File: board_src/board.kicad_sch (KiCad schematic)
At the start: 42 parts, among them J1 Conn_01x05, J16 Conn_01x05, J17 Conn_01x05, J18 Conn_02x20_Counter_Clockwise, J2 Conn_01x05, J20 Conn_02x20_Counter_Clockwise, J21 Conn_02x20_Counter_Clockwise, J22 Conn_02x20_Counter_Clockwise, J26 Conn_01x20_Socket, J27 Conn_01x20_Socket, J30 Conn_01x05, J31 Conn_01x05, J36 Conn_01x20_Socket, J37 Conn_01x20_Socket, J40 Conn_01x01_Pin, J41 Conn_01x01_Pin, J42 Conn_01x01_Pin, J43 Conn_01x01_Pin, J44 Conn_01x01_Pin, J46 Conn_01x01_Pin, U1 Pico, U4 Pico

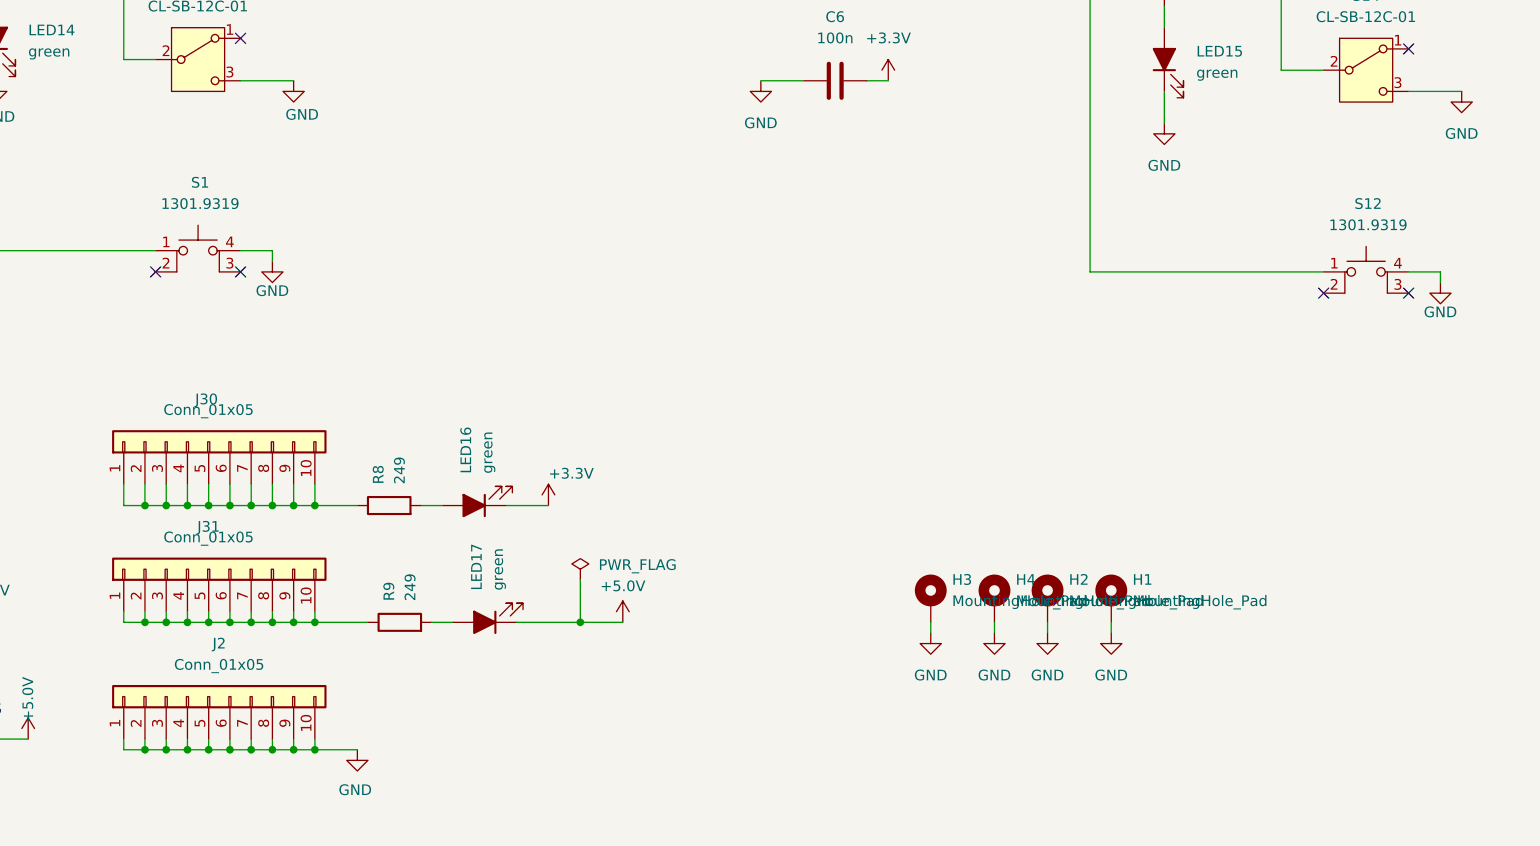
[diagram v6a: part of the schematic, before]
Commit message: poprawione polaczenia diod i wartosci opornikow, aktualizacja niektorych elementow ze wzgledu na braki w magazynie
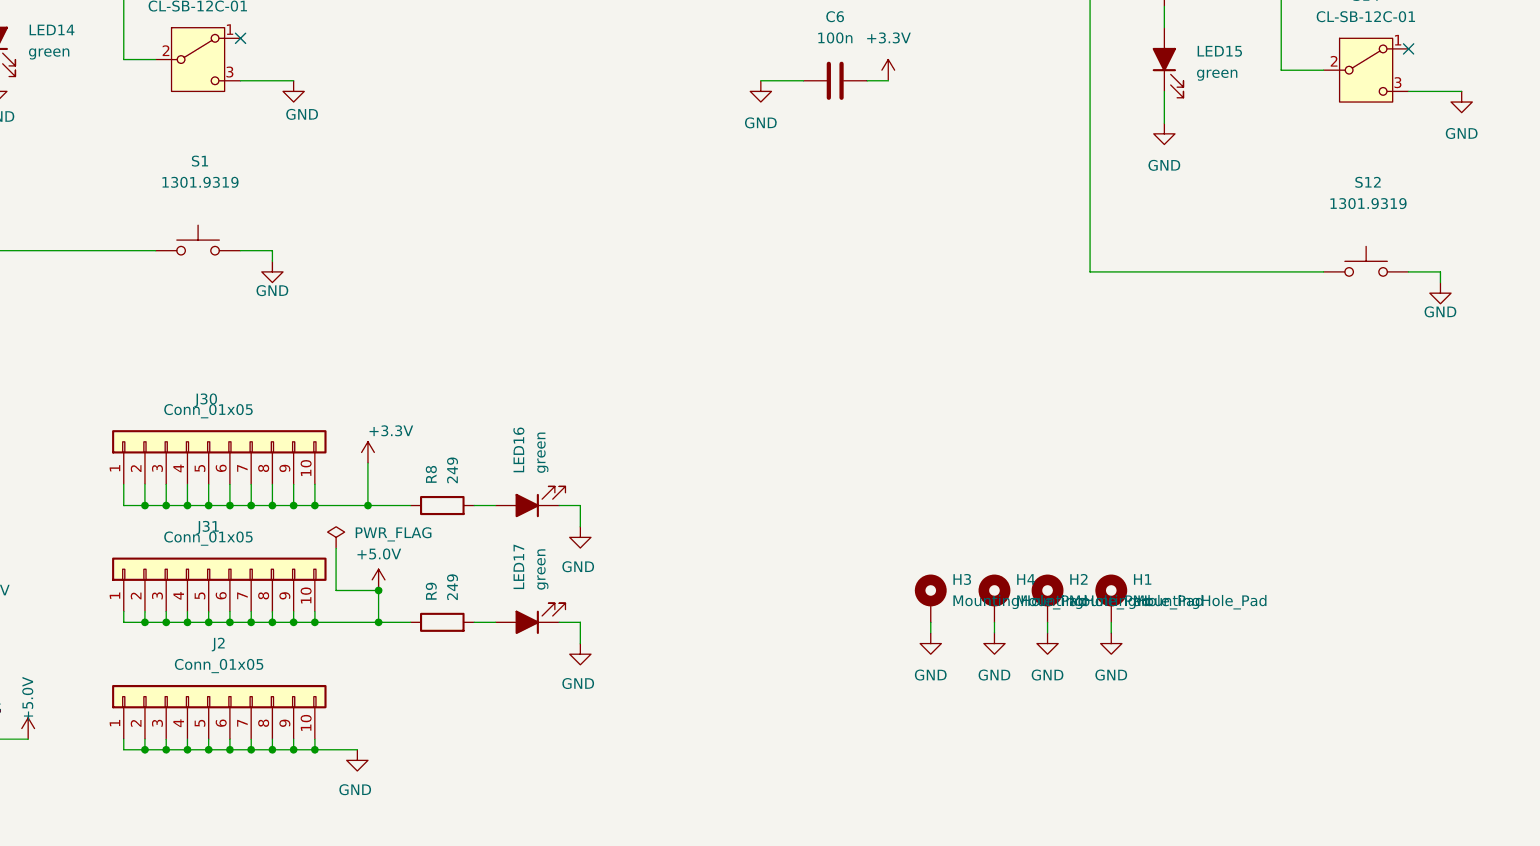
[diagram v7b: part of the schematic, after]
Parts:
- S1, S12: symbol Switch:SW_MEC_5E -> Switch:SW_Push
- S11, S14: footprint footprints:CLSB12C01 -> footprints:JS102011CQN
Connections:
- net +3.3V: now also J30.1 (Pin_1), J30.10 (Pin_10), J30.2 (Pin_2), J30.3 (Pin_3), J30.4 (Pin_4), J30.5 (Pin_5), J30.6 (Pin_6), J30.7 (Pin_7), J30.8 (Pin_8), J30.9 (Pin_9), R8.1; no longer LED16.1 (K)
- net +5.0V: now also J31.1 (Pin_1), J31.10 (Pin_10), J31.2 (Pin_2), J31.3 (Pin_3), J31.4 (Pin_4), J31.5 (Pin_5), J31.6 (Pin_6), J31.7 (Pin_7), J31.8 (Pin_8), J31.9 (Pin_9), R9.1; no longer LED17.1 (K)
- net GND: now also LED16.1 (K), LED17.1 (K), S1.2, S12.2; no longer S1.4 (A), S12.4 (A)
- no-connect marks 92 -> 88
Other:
- moved on the sheet: LED16, LED17, R8, R9

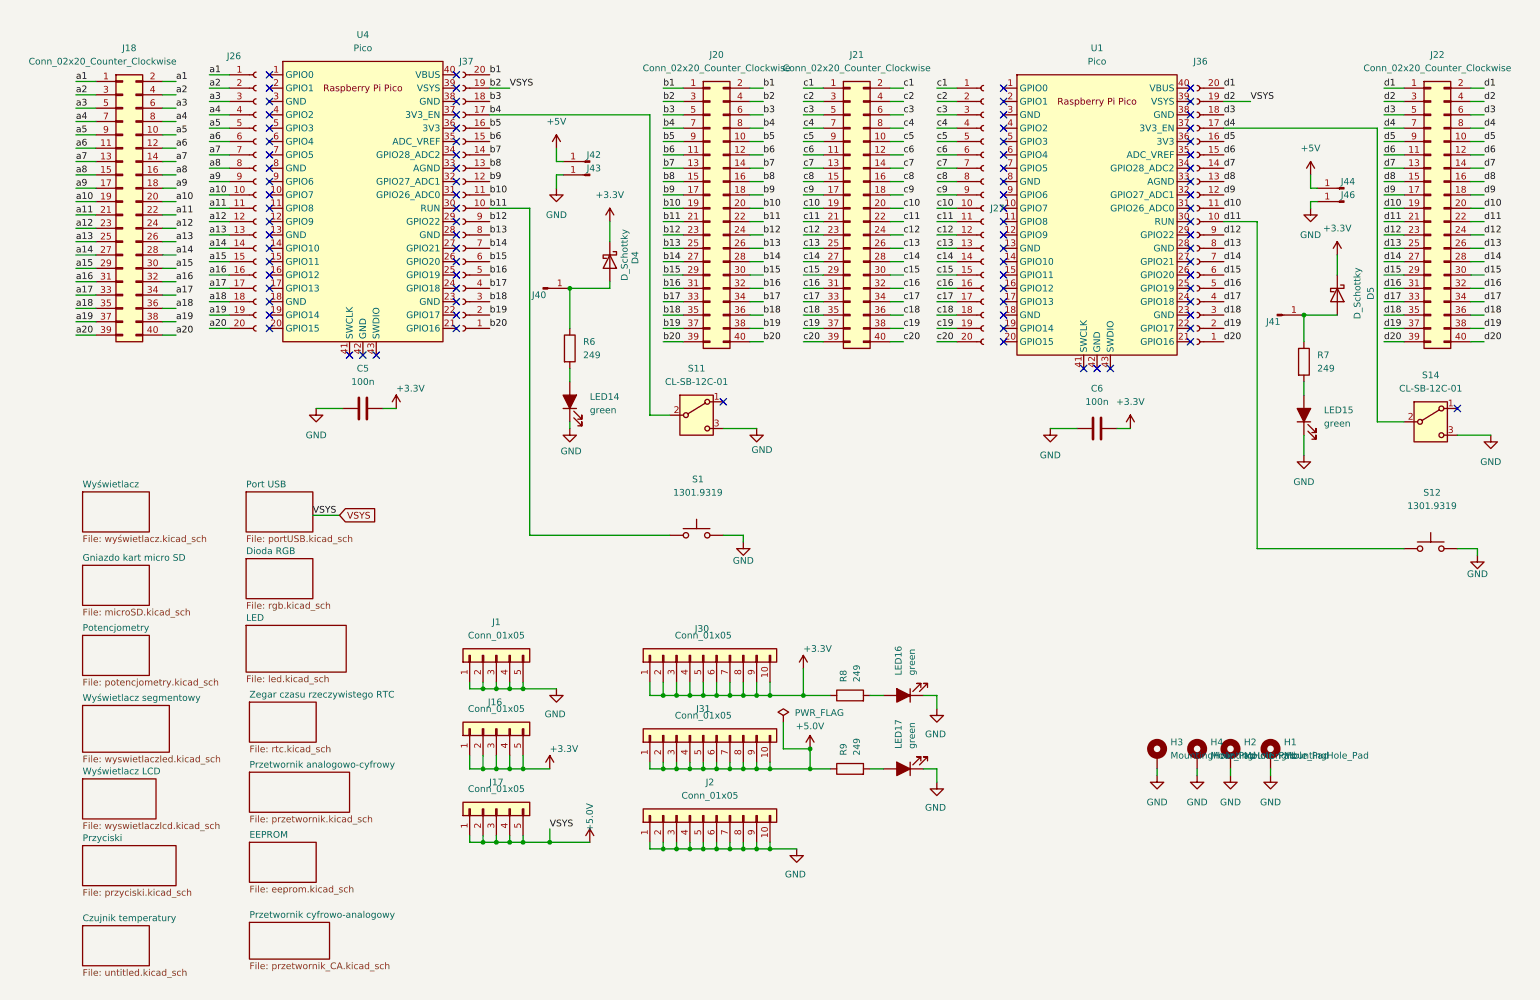
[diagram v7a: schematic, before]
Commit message: dodany tranzystor BS123
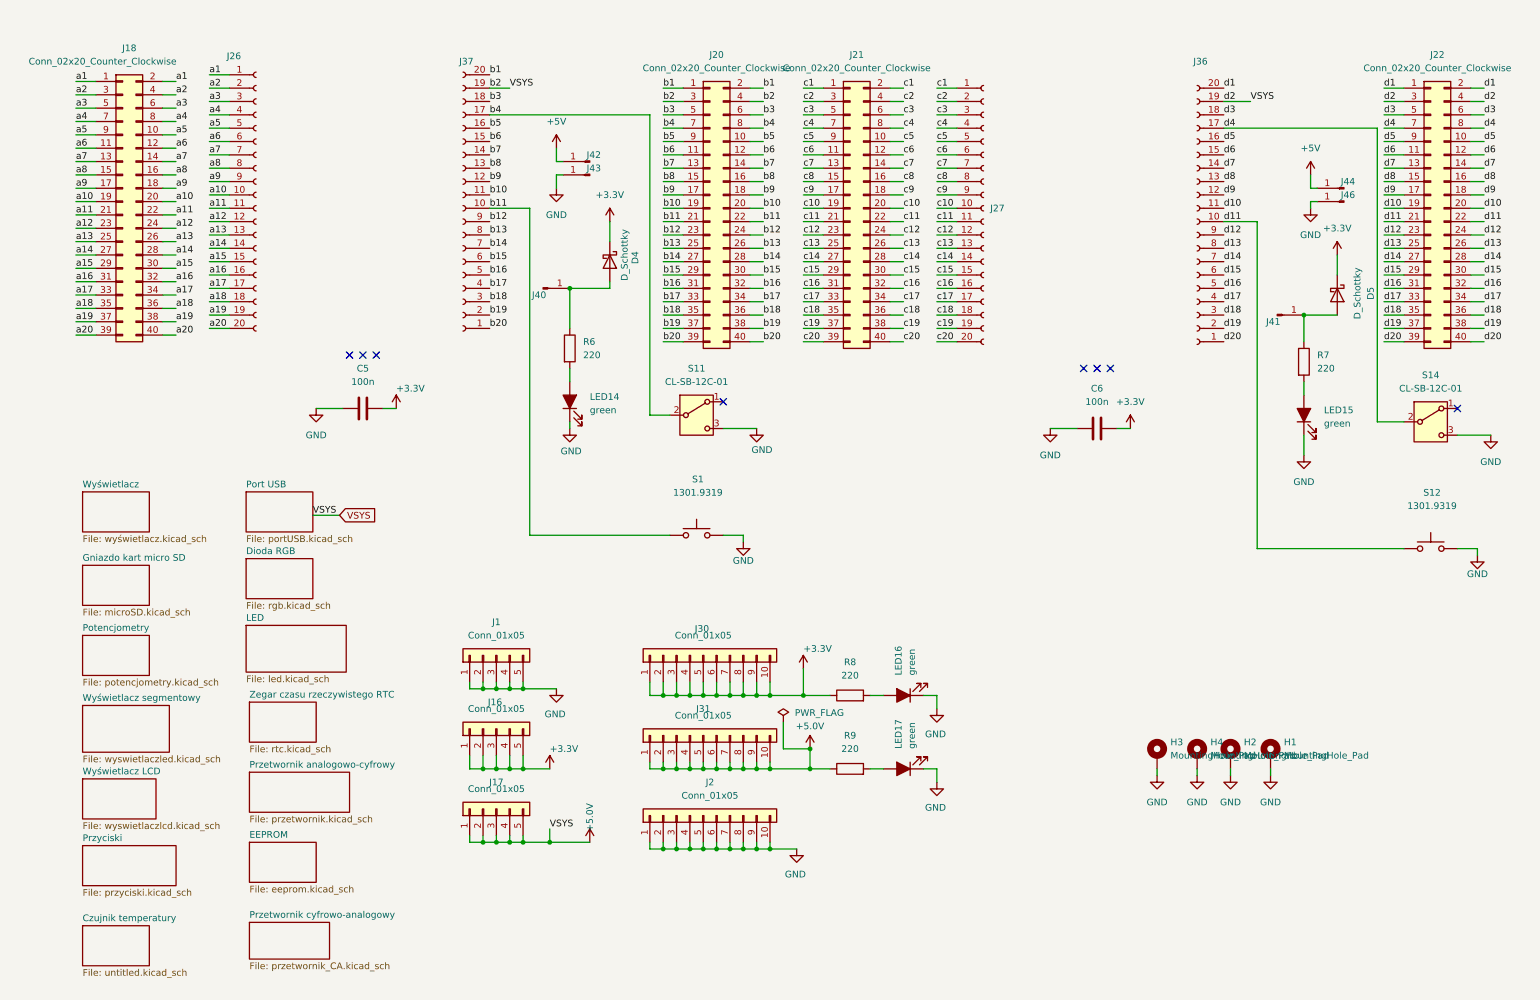
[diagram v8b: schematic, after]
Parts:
- removed U1, U4: Pico, footprints:RPi_Pico_SMD_TH, symbol Raspberry Pi Pico:Pico
- R6, R7, R8, R9: value 249 -> 220
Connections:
- no-connect marks 88 -> 8
